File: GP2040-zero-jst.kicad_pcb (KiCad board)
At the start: 2 copper layers, 47 x 52.5 mm, 16 parts, among them J1 Conn_01x04_Socket, K1 Conn_01x02_Socket, K2 Conn_01x02_Socket, K3 Conn_01x02_Socket, K4 Conn_01x02_Socket, P1 Conn_01x02_Socket, P2 Conn_01x02_Socket, P3 Conn_01x02_Socket, P4 Conn_01x02_Socket

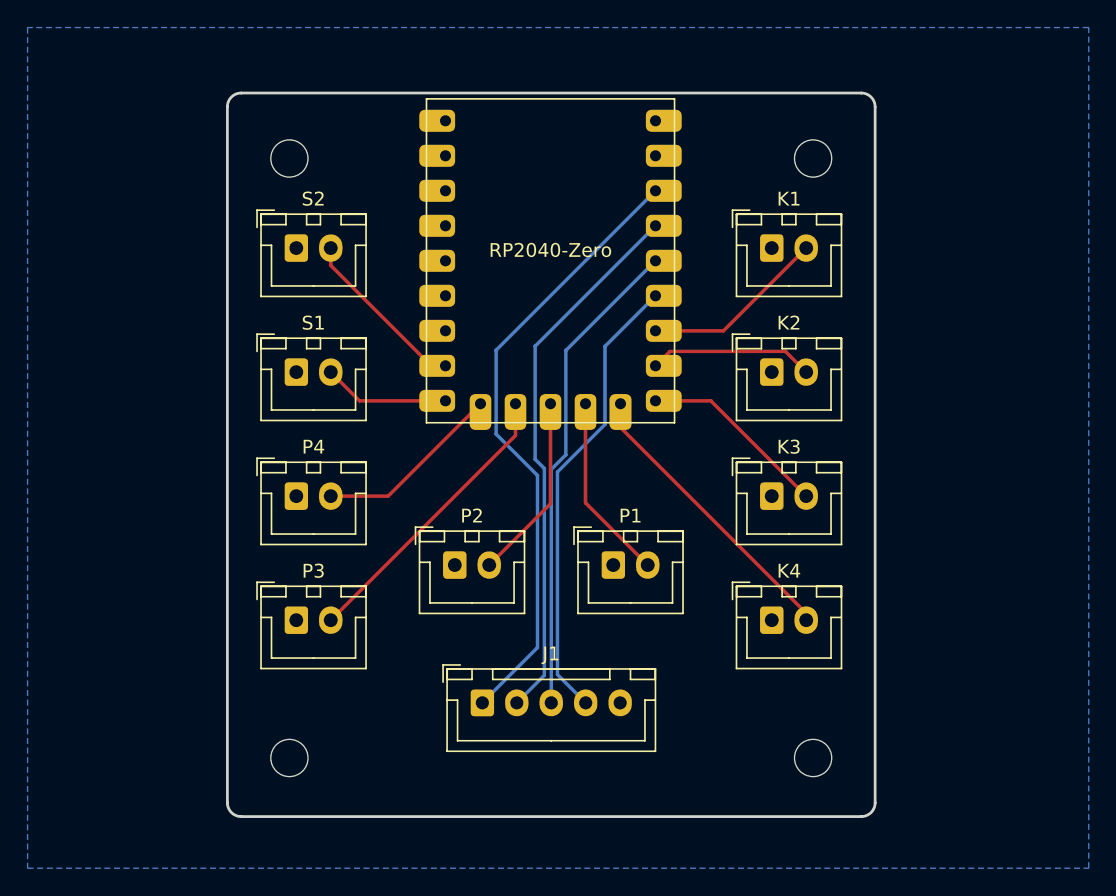
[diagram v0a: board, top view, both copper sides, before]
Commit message: Widen mounting holes, rewire for no-config
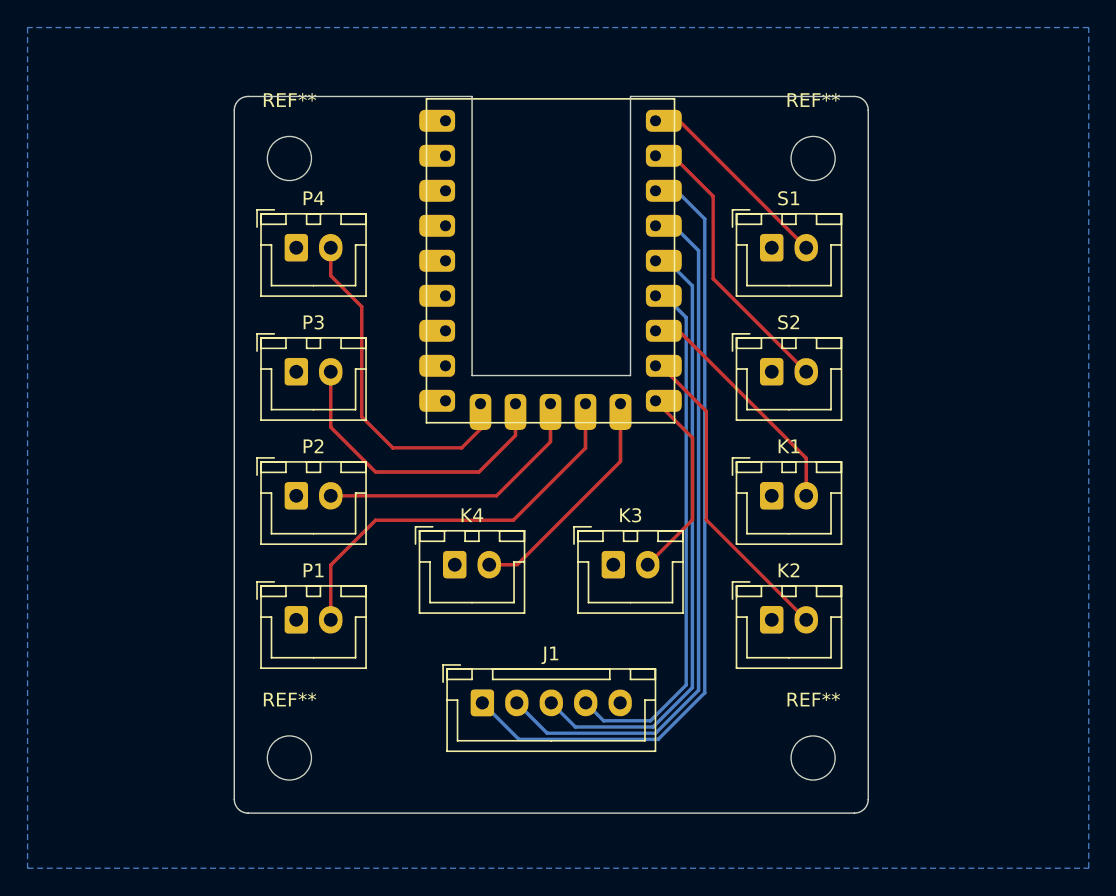
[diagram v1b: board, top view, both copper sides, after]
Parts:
- REF** (x4): value MountingHole_2.7mm_M2.5 -> MountingHole_3.2mm_M3; footprint MountingHole:MountingHole_2.7mm_M2.5 -> MountingHole:MountingHole_3.2mm_M3
- moved S1 35.7 mm to (200.0, 56.0)
- moved S2 35.6 mm to (200.0, 65.0)
- moved K4 23.3 mm to (177.0, 79.0)
- moved P1 23.3 mm to (165.5, 83.0)
- moved P3 18.0 mm to (165.5, 65.0)
- moved P4 18.0 mm to (165.5, 56.0)
- moved K1 18.0 mm to (200.0, 74.0)
- moved K2 18.0 mm to (200.0, 83.0)
- moved P2 12.5 mm to (165.5, 74.0)
- moved K3 12.5 mm to (188.5, 79.0)
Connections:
- RZ1 pad 1: unconnected-(RZ1-GP0-Pad1) -> /S1
- RZ1 pad 15: /S1 -> unconnected-(RZ1-GP14-Pad15)
- RZ1 pad 16: /S2 -> unconnected-(RZ1-GP15-Pad16)
- RZ1 pad 2: unconnected-(RZ1-GP1-Pad2) -> /S2
- RZ1 pad 23: /COM -> unconnected-(RZ1-VSYS-Pad23)
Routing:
- net /1P: track 13.6 -> 29.2 mm
- net /UP: track 44.8 -> 57.4 mm
- net /DOWN: track 39.3 -> 51.2 mm
- net /4P: track 13.6 -> 25.2 mm
- net /2K: track 12.0 -> 23.2 mm
- net /RIGHT: track 35.2 -> 44.7 mm
- net /S2: track 12.6 -> 20.9 mm
- net /2P: track 13.5 -> 20.3 mm
- net /S1: track 9.19 -> 14.7 mm
- net /LEFT: track 33.3 -> 38.4 mm
- net /4K: track 21.3 -> 16.8 mm
- net /1K: track 13.4 -> 17.5 mm
- net /3P: track 21.3 -> 22.2 mm
- net /3K: track 13.8 -> 14.3 mm
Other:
- board size 47 x 52.5 mm -> 46 x 52 mm
